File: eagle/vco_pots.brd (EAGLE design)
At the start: 100 x 80 mm, 18 parts, among them P1 P0915N, P10 P0915N, P2 P0915N, P3 P0915N, P4 P0915N, P5 P0915N, P6 P0915N, P7 P0915N, P8 P0915N, P9 P0915N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

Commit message: corrected jumper between sliders
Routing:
- net GND: track 334.4 -> 338.2 mm
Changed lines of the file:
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@@
 <wire x1="86.4" y1="28.06" x2="86.4" y2="42.03" width="0.8128" layer="16"/>
 <wire x1="86.4" y1="14.09" x2="86.4" y2="28.06" width="0.8128" layer="16"/>
-<via x="35.56" y="53.34" extent="1-16" drill="0.8" shape="square"/>
-<wire x1="35.56" y1="53.34" x2="35.56" y2="58.42" width="0.8128" layer="1"/>
-<via x="35.56" y="58.42" extent="1-16" drill="0.8" shape="square"/>
-<wire x1="35.56" y1="58.42" x2="12.7" y2="58.42" width="0.8128" layer="16"/>
+<via x="31.75" y="53.34" extent="1-16" drill="0.8" shape="square"/>
+<wire x1="31.75" y1="53.34" x2="31.75" y2="58.42" width="0.8128" layer="1"/>
+<via x="31.75" y="58.42" extent="1-16" drill="0.8" shape="square"/>
+<wire x1="31.75" y1="58.42" x2="12.7" y2="58.42" width="0.8128" layer="16"/>
 <via x="12.7" y="58.42" extent="1-16" drill="0.8" shape="square"/>
 <wire x1="12.7" y1="58.42" x2="7.62" y2="58.42" width="0.8128" layer="1"/>
@@
 <wire x1="61.75" y1="27.785" x2="61.75" y2="53.82" width="0.8128" layer="16"/>
 <wire x1="61.75" y1="53.82" x2="57.15" y2="58.42" width="0.8128" layer="16"/>
-<wire x1="57.15" y1="58.42" x2="35.56" y2="58.42" width="0.8128" layer="16"/>
-<wire x1="35.56" y1="53.34" x2="35.56" y2="52.07" width="0.8128" layer="16"/>
-<wire x1="35.56" y1="52.07" x2="45.72" y2="41.91" width="0.8128" layer="16"/>
-<wire x1="45.72" y1="41.91" x2="48.18" y2="41.91" width="0.8128" layer="16"/>
+<wire x1="57.15" y1="58.42" x2="31.75" y2="58.42" width="0.8128" layer="16"/>
+<wire x1="31.75" y1="53.34" x2="31.75" y2="52.07" width="0.8128" layer="16"/>
+<wire x1="31.75" y1="52.07" x2="41.91" y2="41.91" width="0.8128" layer="16"/>
+<wire x1="41.91" y1="41.91" x2="48.18" y2="41.91" width="0.8128" layer="16"/>
 <wire x1="48.18" y1="41.91" x2="48.3" y2="42.03" width="0.8128" layer="16"/>
 <wire x1="23.65" y1="15.08" x2="23.65" y2="22.38" width="0.8128" layer="16"/>

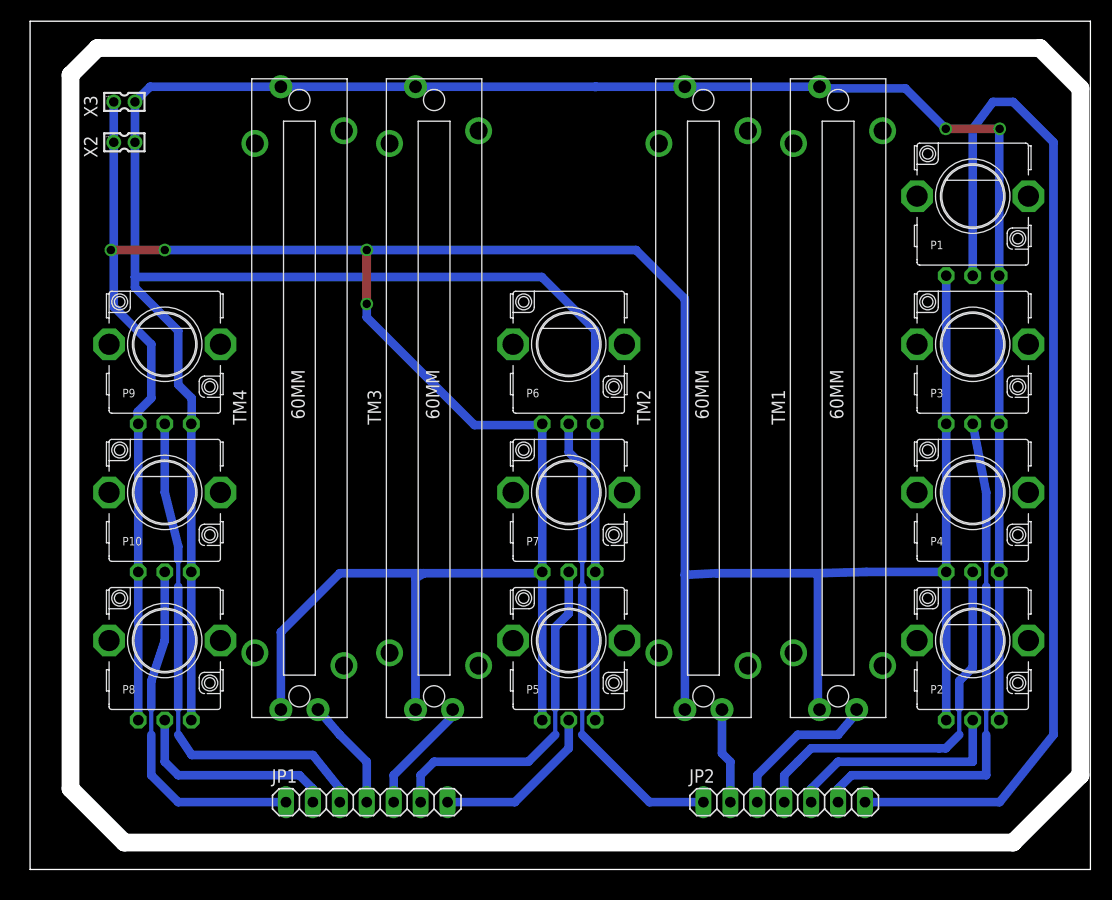
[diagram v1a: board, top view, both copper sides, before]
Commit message: moved pcb to zero corner
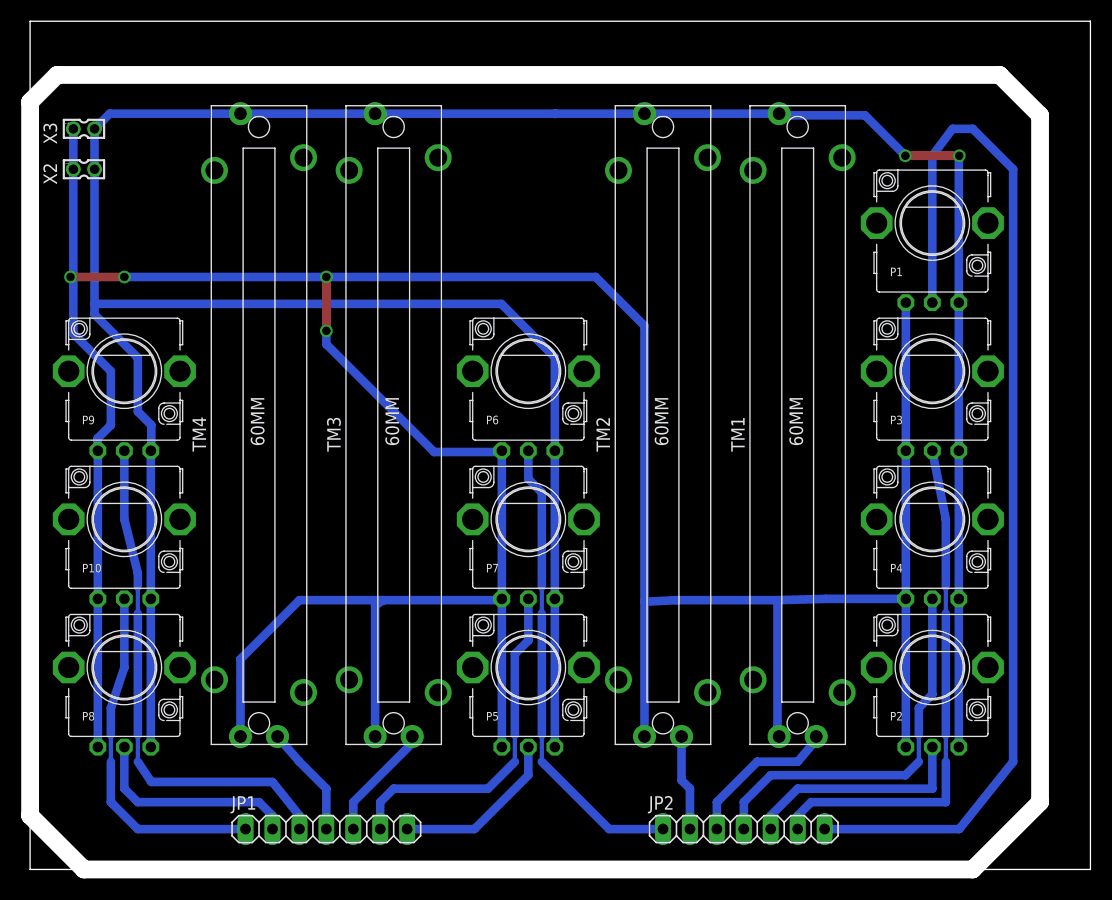
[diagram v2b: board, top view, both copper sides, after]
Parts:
- moved TM1 4.58 mm to (72.4, 41.9)
- moved TM2 4.58 mm to (59.7, 41.9)
- moved TM3 4.58 mm to (34.3, 41.9)
- moved X3 4.58 mm to (5.08, 69.8)
- moved JP2 4.58 mm to (67.3, 3.81)
- moved P1 4.58 mm to (85.1, 61.0)
- moved P2 4.58 mm to (85.1, 19.1)
- moved P3 4.58 mm to (85.1, 47.0)
- moved P4 4.58 mm to (85.1, 33.0)
- moved TM4 4.58 mm to (21.6, 41.9)
- moved JP1 4.58 mm to (27.9, 3.81)
- moved P10 4.58 mm to (8.89, 33.0)
- moved P8 4.58 mm to (8.89, 19.1)
- moved P9 4.58 mm to (8.89, 47.0)
- moved P5 4.58 mm to (47.0, 19.1)
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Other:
- outline, holes or cut-outs redrawn
